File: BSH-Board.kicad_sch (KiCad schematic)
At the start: 35 parts, among them J1 667101210103, J2 MICRO QTZB5.0, SW1 TS-3025-B-C-B, SW2 TS-3025-B-C-B, U1 ESP32-C6-MINI-1-N4, U2 AP63203WU, U3 NCP715SQ50T2G, U4 TXS0102DQER

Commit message: Next attempt
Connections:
- net D-BUS: now also R1.2, U4.2 (A1), U4.3 (A2); no longer J1.A2, J1.B2, R1.1
- new net: J1.A2, J1.B2, R1.1
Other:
- moved on the sheet: D2, R1
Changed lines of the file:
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@@
 	(wire
 		(pts
-			(xy 114.3 41.91) (xy 107.95 41.91)
+			(xy 123.19 41.91) (xy 130.81 41.91)
 		)
 		(stroke
@@
 	(wire
 		(pts
-			(xy 73.66 41.91) (xy 77.47 41.91)
+			(xy 87.63 41.91) (xy 91.44 41.91)
 		)
 		(stroke
@@
 	(wire
 		(pts
-			(xy 130.81 41.91) (xy 119.38 41.91)
+			(xy 128.27 99.06) (xy 146.05 99.06)
 		)
 		(stroke
@@
 	(wire
 		(pts
-			(xy 128.27 99.06) (xy 146.05 99.06)
+			(xy 233.68 115.57) (xy 233.68 118.11)
 		)
 		(stroke
@@
 	(wire
 		(pts
-			(xy 233.68 115.57) (xy 233.68 118.11)
+			(xy 243.84 77.47) (xy 243.84 83.82)
 		)
 		(stroke
@@
 	(wire
 		(pts
-			(xy 243.84 77.47) (xy 243.84 83.82)
+			(xy 146.05 99.06) (xy 146.05 100.33)
 		)
 		(stroke
@@
 	(wire
 		(pts
-			(xy 146.05 99.06) (xy 146.05 100.33)
+			(xy 128.27 26.67) (xy 128.27 31.75)
 		)
 		(stroke
@@
 	(wire
 		(pts
-			(xy 128.27 26.67) (xy 128.27 31.75)
+			(xy 133.35 43.18) (xy 130.81 43.18)
 		)
 		(stroke
@@
 	(wire
 		(pts
-			(xy 133.35 43.18) (xy 130.81 43.18)
+			(xy 54.61 41.91) (xy 62.23 41.91)
 		)
 		(stroke
@@
 	(wire
 		(pts
-			(xy 35.56 41.91) (xy 48.26 41.91)
+			(xy 35.56 41.91) (xy 49.53 41.91)
 		)
 		(stroke
@@
 	(wire
 		(pts
-			(xy 82.55 49.53) (xy 82.55 53.34)
+			(xy 96.52 49.53) (xy 96.52 53.34)
 		)
 		(stroke
@@
 	(wire
 		(pts
-			(xy 82.55 26.67) (xy 82.55 34.29)
+			(xy 96.52 26.67) (xy 96.52 34.29)
 		)
 		(stroke
@@
 	(global_label "D-BUS"
 		(shape input)
-		(at 48.26 41.91 0)
+		(at 62.23 41.91 0)
 		(fields_autoplaced yes)
 		(effects
@@
 		)
 		(property "Intersheetrefs" "${INTERSHEET_REFS}"
-			(at 57.8976 41.91 0)
+			(at 71.8676 41.91 0)
 			(effects
 				(font
@@
 	(global_label "D-BUS"
 		(shape input)
-		(at 73.66 41.91 180)
+		(at 87.63 41.91 180)
 		(fields_autoplaced yes)
 		(effects
@@
 		)
 		(property "Intersheetrefs" "${INTERSHEET_REFS}"
-			(at 64.0224 41.91 0)
+			(at 77.9924 41.91 0)
 			(effects
 				(font
@@
 	(global_label "D-BUS"
 		(shape input)
-		(at 107.95 41.91 180)
+		(at 123.19 41.91 180)
 		(fields_autoplaced yes)
 		(effects
@@
 		)
 		(property "Intersheetrefs" "${INTERSHEET_REFS}"
-			(at 98.3124 41.91 0)
+			(at 113.5524 41.91 0)
 			(effects
 				(font
@@
 	(symbol
 		(lib_id "power:+5V")
-		(at 82.55 26.67 0)
+		(at 96.52 26.67 0)
 		(mirror y)
 		(unit 1)
@@
 		(fields_autoplaced yes)
 		(property "Reference" "#PWR012"
-			(at 82.55 30.48 0)
+			(at 96.52 30.48 0)
 			(effects
 				(font
@@
 		)
 		(property "Value" "+5V"
-			(at 82.55 21.59 0)
+			(at 96.52 21.59 0)
 			(effects
 				(font
@@
 		)
 		(property "Footprint" ""
-			(at 82.55 26.67 0)
+			(at 96.52 26.67 0)
 			(effects
 				(font
@@
 		)
 		(property "Datasheet" ""
-			(at 82.55 26.67 0)
+			(at 96.52 26.67 0)
 			(effects
 				(font
@@
 		)
 		(property "Description" "Power symbol creates a global label with name \"+5V\""
-			(at 82.55 26.67 0)
+			(at 96.52 26.67 0)
 			(effects
 				(font
@@
 	(symbol
 		(lib_id "Diode:BAV99")
-		(at 82.55 41.91 270)
+		(at 96.52 41.91 270)
 		(mirror x)
 		(unit 1)
@@
 		(fields_autoplaced yes)
 		(property "Reference" "D2"
-			(at 85.09 40.6399 90)
+			(at 99.06 40.6399 90)
 			(effects
 				(font
@@
 		)
 		(property "Value" "BAV99,215"
-			(at 85.09 43.1799 90)
+			(at 99.06 43.1799 90)
 			(effects
 				(font
@@
 		)
 		(property "Footprint" "Package_TO_SOT_SMD:SOT-23"
-			(at 69.85 41.91 0)
+			(at 83.82 41.91 0)
 			(effects
 				(font
@@
 		)
 		(property "Datasheet" "https://assets.nexperia.com/documents/data-sheet/BAV99_SER.pdf"
-			(at 82.55 41.91 0)
+			(at 96.52 41.91 0)
 			(effects
 				(font
@@
 		)
 		(property "Description" "BAV99 High-speed switching diodes, SOT-23"
-			(at 82.55 41.91 0)
+			(at 96.52 41.91 0)
 			(effects
 				(font
@@
 	(symbol
 		(lib_id "Device:R_Small")
-		(at 116.84 41.91 90)
+		(at 52.07 41.91 90)
 		(unit 1)
 		(exclude_from_sim no)
@@
 		(dnp no)
 		(property "Reference" "R1"
-			(at 116.84 40.132 90)
+			(at 52.07 40.132 90)
 			(effects
 				(font
@@
 		)
 		(property "Value" "120"
-			(at 116.84 43.942 90)
+			(at 52.07 43.942 90)
 			(effects
 				(font
@@
 		)
 		(property "Footprint" "Resistor_SMD:R_0402_1005Metric"
-			(at 116.84 41.91 0)
+			(at 52.07 41.91 0)
 			(effects
 				(font
@@
 		)
 		(property "Datasheet" "~"
-			(at 116.84 41.91 0)
+			(at 52.07 41.91 0)
 			(effects
 				(font
@@
 		)
 		(property "Description" "Resistor, small symbol"
-			(at 116.84 41.91 0)
+			(at 52.07 41.91 0)
 			(effects
 				(font
@@
 		)
 		(property "LCSC" "C25079"
-			(at 116.84 41.91 90)
+			(at 52.07 41.91 90)
 			(effects
 				(font
@@
 		)
 		(instances
-			(project ""
+			(project "BSH-Board"
 				(path "/a694a5cb-1269-46af-95fb-e7b464b1f747"
 					(reference "R1")
@@
 	(symbol
 		(lib_id "power:GND")
-		(at 82.55 53.34 0)
+		(at 96.52 53.34 0)
 		(unit 1)
 		(exclude_from_sim no)
@@
 		(fields_autoplaced yes)
 		(property "Reference" "#PWR016"
-			(at 82.55 59.69 0)
+			(at 96.52 59.69 0)
 			(effects
 				(font
@@
 		)
 		(property "Value" "GND"
-			(at 82.55 58.42 0)
+			(at 96.52 58.42 0)
 			(effects
 				(font
@@
 		)
 		(property "Footprint" ""
-			(at 82.55 53.34 0)
+			(at 96.52 53.34 0)
 			(effects
 				(font
@@
 		)
 		(property "Datasheet" ""
-			(at 82.55 53.34 0)
+			(at 96.52 53.34 0)
 			(effects
 				(font
@@
 		)
 		(property "Description" "Power symbol creates a global label with name \"GND\" , ground"
-			(at 82.55 53.34 0)
+			(at 96.52 53.34 0)
 			(effects
 				(font

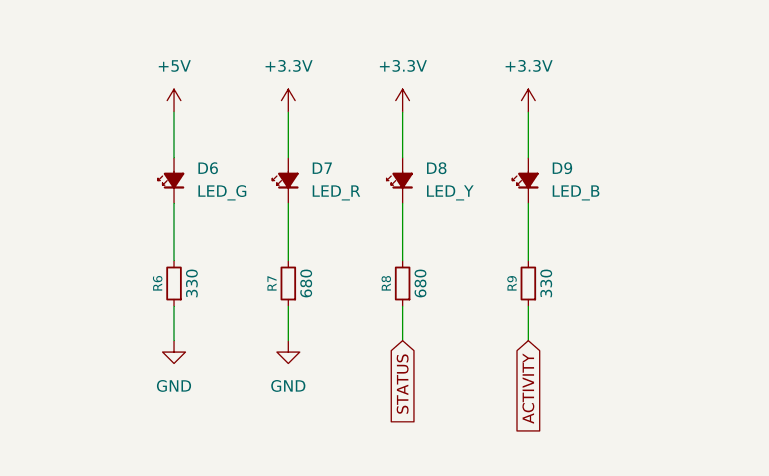
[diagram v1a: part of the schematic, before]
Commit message: Fixed some issues, added missing JLC part numbers
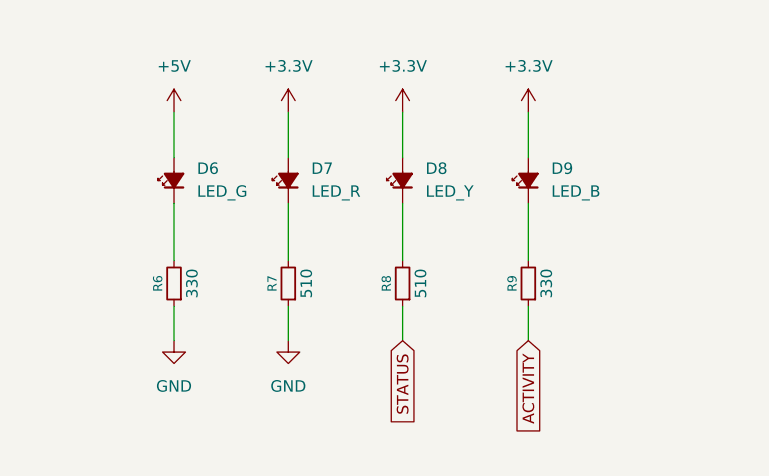
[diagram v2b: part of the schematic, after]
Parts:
- D2: LCSC (none) -> C2500
- J1: now left out of the parts list
- R7, R8: value 680 -> 510; LCSC C25079 -> C25123
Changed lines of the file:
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@@
+			)
+		)
+		(property "LCSC" "C2500"
+			(at 96.52 41.91 90)
+			(effects
+				(font
+					(size 1.27 1.27)
+				)
+				(hide yes)
 			)
 		)
@@
 		(unit 1)
 		(exclude_from_sim no)
-		(in_bom yes)
+		(in_bom no)
 		(on_board yes)
 		(dnp no)
@@
 			)
 		)
-		(property "Value" "680"
+		(property "Value" "510"
 			(at 59.182 156.21 90)
 			(effects
@@
 			)
 		)
-		(property "LCSC" "C25079"
+		(property "LCSC" "C25123"
 			(at 57.15 156.21 90)
 			(effects
@@
 			)
 		)
-		(property "Value" "680"
+		(property "Value" "510"
 			(at 71.882 156.21 90)
 			(effects
@@
 			)
 		)
-		(property "LCSC" "C25079"
+		(property "LCSC" "C25123"
 			(at 69.85 156.21 90)
 			(effects

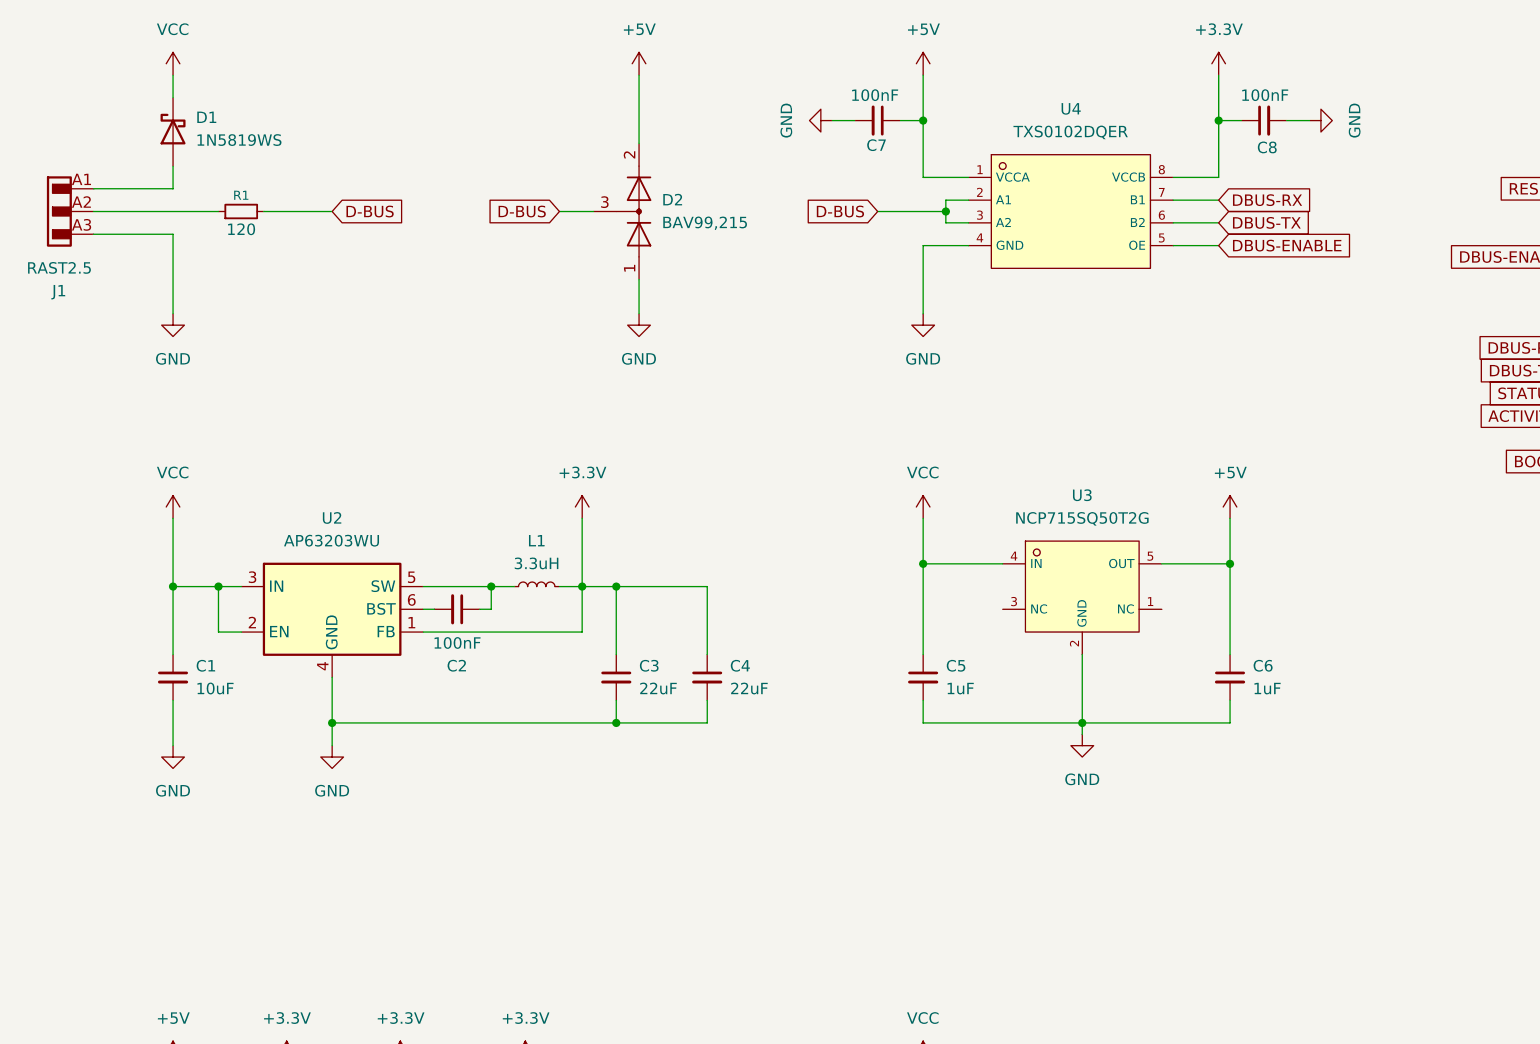
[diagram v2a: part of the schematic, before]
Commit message: Fix TXS0102DQER bug
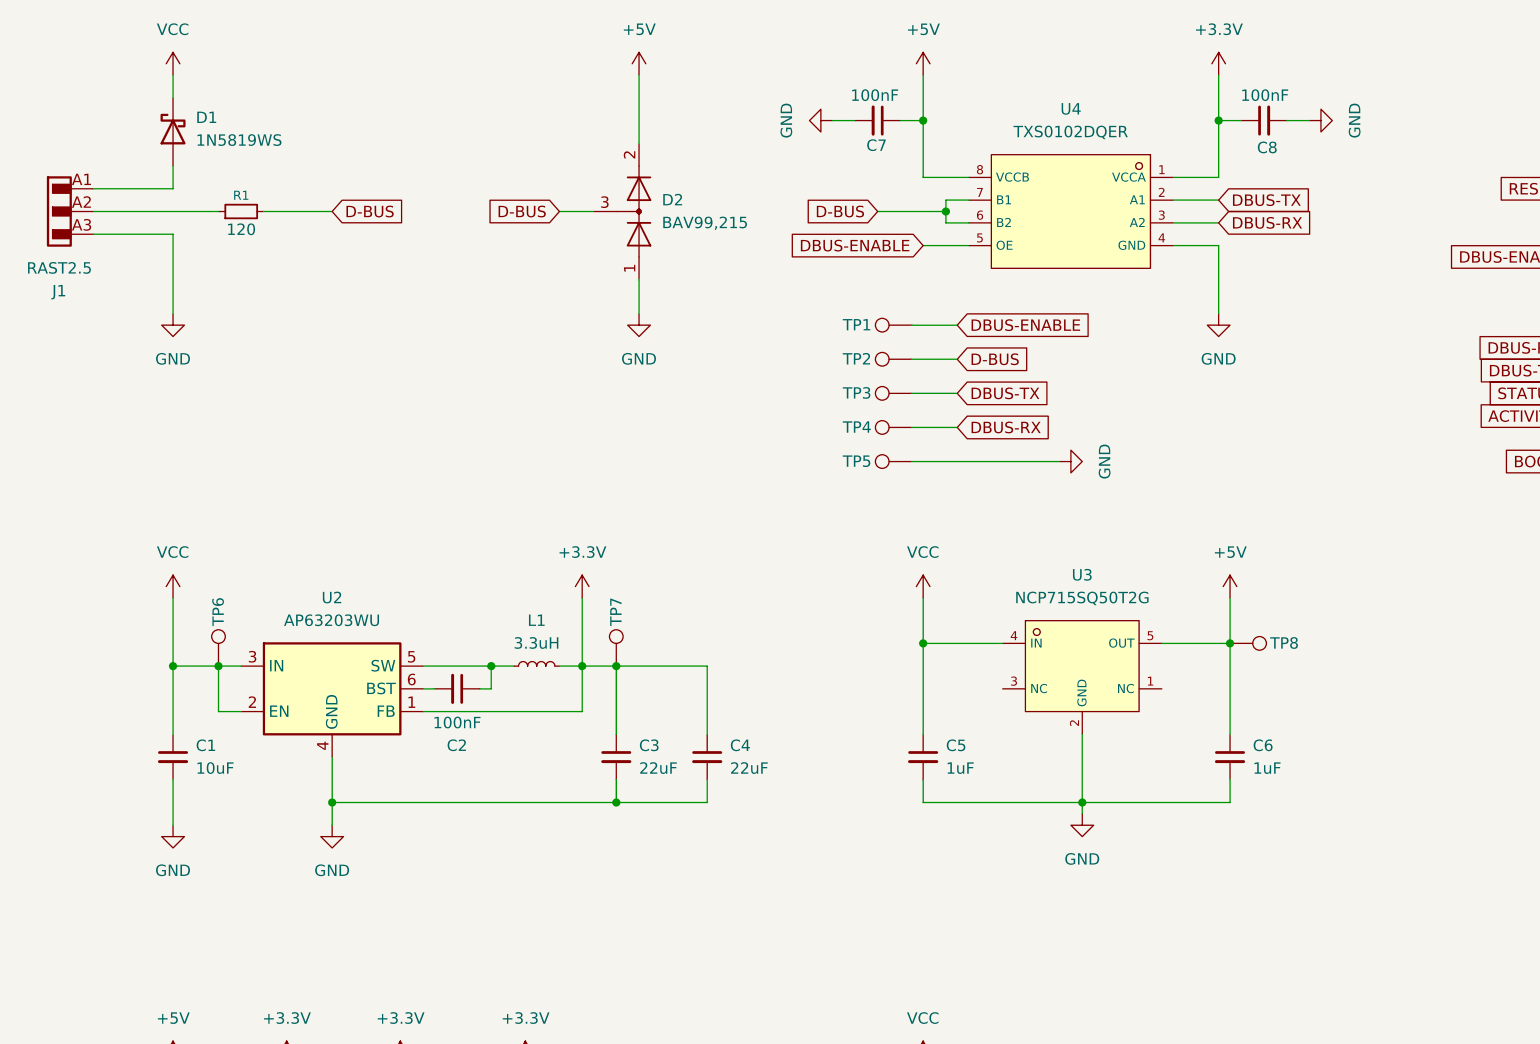
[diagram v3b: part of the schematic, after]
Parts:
- added TP1, TP2, TP3, TP4, TP5, TP6, TP7, TP8: TestPoint, TestPoint:TestPoint_Pad_D1.0mm, symbol Connector:TestPoint
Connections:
- net +3.3V: now also U4.1 (VCCA), TP7.1; no longer U4.8 (VCCB)
- net +5V: now also U4.8 (VCCB), TP8.1; no longer U4.1 (VCCA)
- net D-BUS: now also U4.6 (B2), U4.7 (B1), TP2.1; no longer U4.2 (A1), U4.3 (A2)
- net DBUS-ENABLE: now also TP1.1
- net DBUS-RX: now also U4.3 (A2), TP4.1; no longer U4.7 (B1)
- net DBUS-TX: now also U4.2 (A1), TP3.1; no longer U4.6 (B2)
- net GND: now also TP5.1
- net VCC: now also TP6.1
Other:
- moved on the sheet: C1, C2, C3, C4, C5, C6, L1, U2, U3

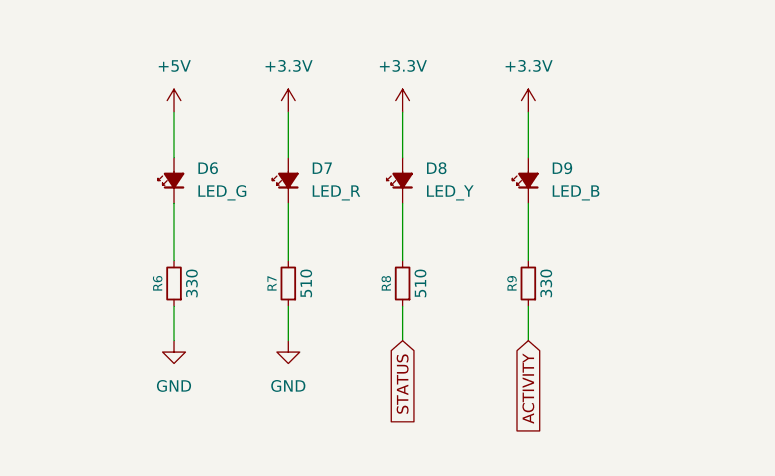
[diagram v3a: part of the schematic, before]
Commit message: Adjusted resistor values for green and blue led
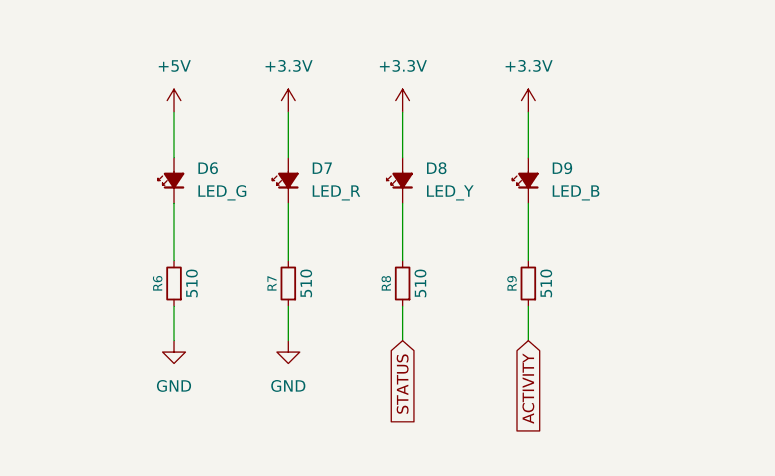
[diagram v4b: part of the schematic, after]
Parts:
- R6, R9: value 330 -> 510; LCSC C25104 -> C25123
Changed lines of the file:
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@@
 			)
 		)
-		(property "Value" "330"
+		(property "Value" "510"
 			(at 46.482 156.21 90)
 			(effects
@@
 			)
 		)
-		(property "LCSC" "C25104"
+		(property "LCSC" "C25123"
 			(at 44.45 156.21 90)
 			(effects
@@
 			)
 		)
-		(property "Value" "330"
+		(property "Value" "510"
 			(at 85.852 156.21 90)
 			(effects
@@
 			)
 		)
-		(property "LCSC" "C25104"
+		(property "LCSC" "C25123"
 			(at 83.82 156.21 90)
 			(effects

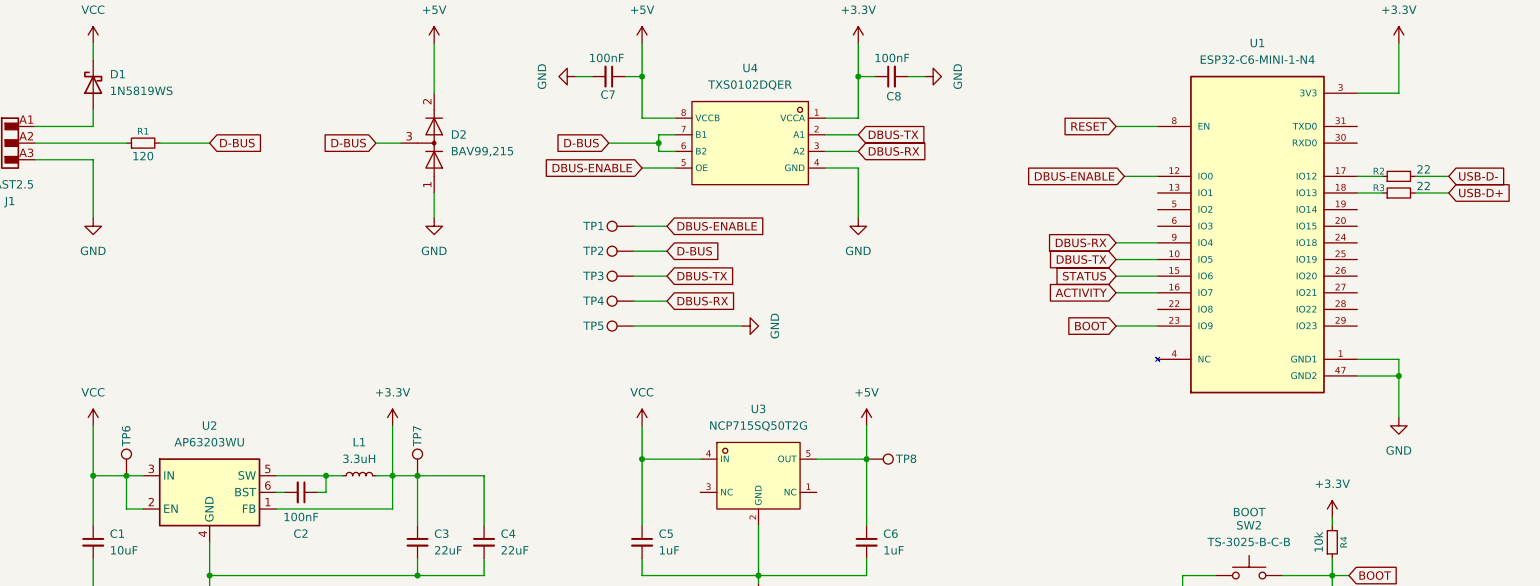
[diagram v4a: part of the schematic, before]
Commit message: TXS0102 OE directly to 3.3v, all spare IOs to Testpoints
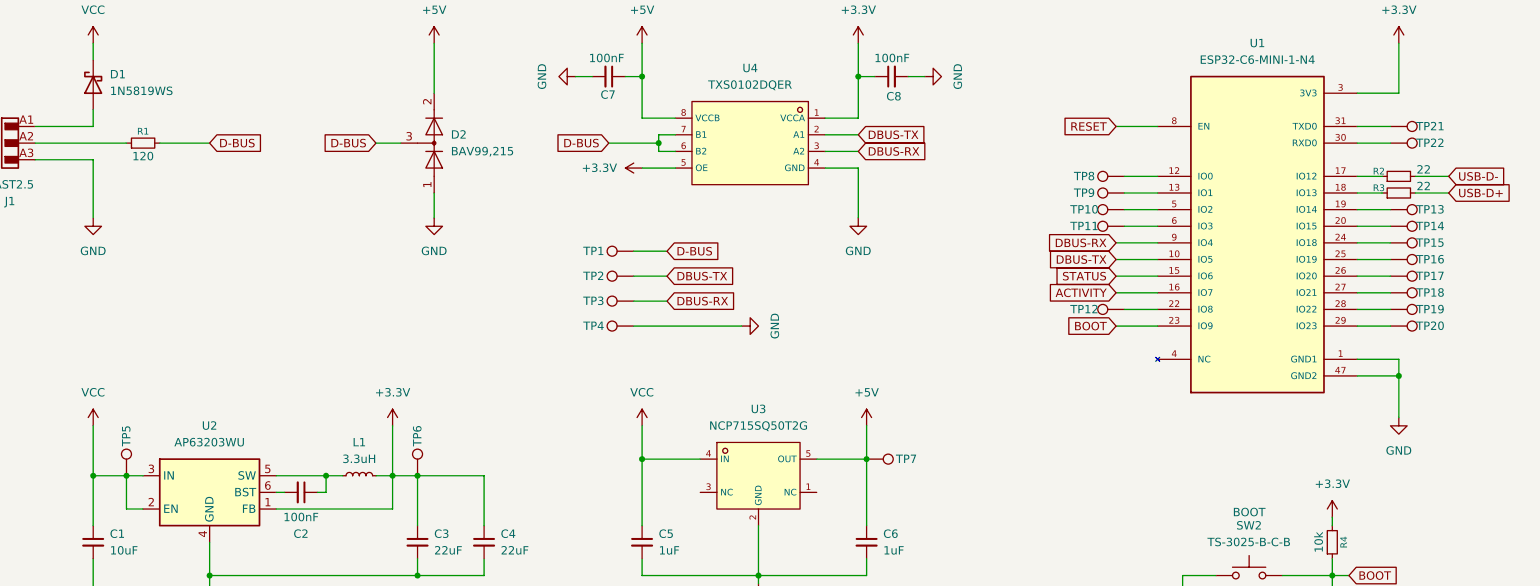
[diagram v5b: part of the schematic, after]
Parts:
- removed TP1: TestPoint, TestPoint:TestPoint_Pad_D1.0mm, symbol Connector:TestPoint
- added TP10, TP11, TP12, TP13, TP14, TP15, TP16, TP17, TP18, TP19, TP20, TP21, TP22, TP8, TP9: TestPoint, Testpoints:TestPoint_Pad_D1.0mm, symbol Connector:TestPoint
- TP1: renamed from TP2; footprint TestPoint:TestPoint_Pad_D1.0mm -> Testpoints:TestPoint_Pad_D1.0mm
- TP2: renamed from TP3; footprint TestPoint:TestPoint_Pad_D1.0mm -> Testpoints:TestPoint_Pad_D1.0mm
- TP3: renamed from TP4; footprint TestPoint:TestPoint_Pad_D1.0mm -> Testpoints:TestPoint_Pad_D1.0mm
- TP4: renamed from TP5; footprint TestPoint:TestPoint_Pad_D1.0mm -> Testpoints:TestPoint_Pad_D1.0mm
- TP5: renamed from TP6; footprint TestPoint:TestPoint_Pad_D1.0mm -> Testpoints:TestPoint_Pad_D1.0mm
- TP6: renamed from TP7; footprint TestPoint:TestPoint_Pad_D1.0mm -> Testpoints:TestPoint_Pad_D1.0mm
- TP7: renamed from TP8; footprint TestPoint:TestPoint_Pad_D1.0mm -> Testpoints:TestPoint_Pad_D1.0mm
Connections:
- net +3.3V: now also U4.5 (OE)
- net at U1.13 (IO1): now also TP9.1
- net at U1.19 (IO14): now also TP13.1
- net at U1.20 (IO15): now also TP14.1
- net at U1.22 (IO8): now also TP12.1
- net at U1.24 (IO18): now also TP15.1
- net at U1.25 (IO19): now also TP16.1
- net at U1.26 (IO20): now also TP17.1
- net at U1.27 (IO21): now also TP18.1
- net at U1.28 (IO22): now also TP19.1
- net at U1.29 (IO23): now also TP20.1
- net at U1.30 (RXD0): now also TP22.1
- net at U1.31 (TXD0): now also TP21.1
- net at U1.5 (IO2): now also TP10.1
- net at U1.6 (IO3): now also TP11.1
- net DBUS-ENABLE: no longer names the net of U1.12 (IO0)
- net DBUS-ENABLE: now also TP8.1; no longer U4.5 (OE)
